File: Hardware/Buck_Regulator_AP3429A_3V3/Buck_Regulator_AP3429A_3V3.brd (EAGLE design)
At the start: 25.4 x 25.4 mm, 51 parts, among them J1 Screw Terminal, J2 POWER_JACKPOWER_JACK_SLOT_COM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, J3 Breakout Headers, U1 AP3429/A

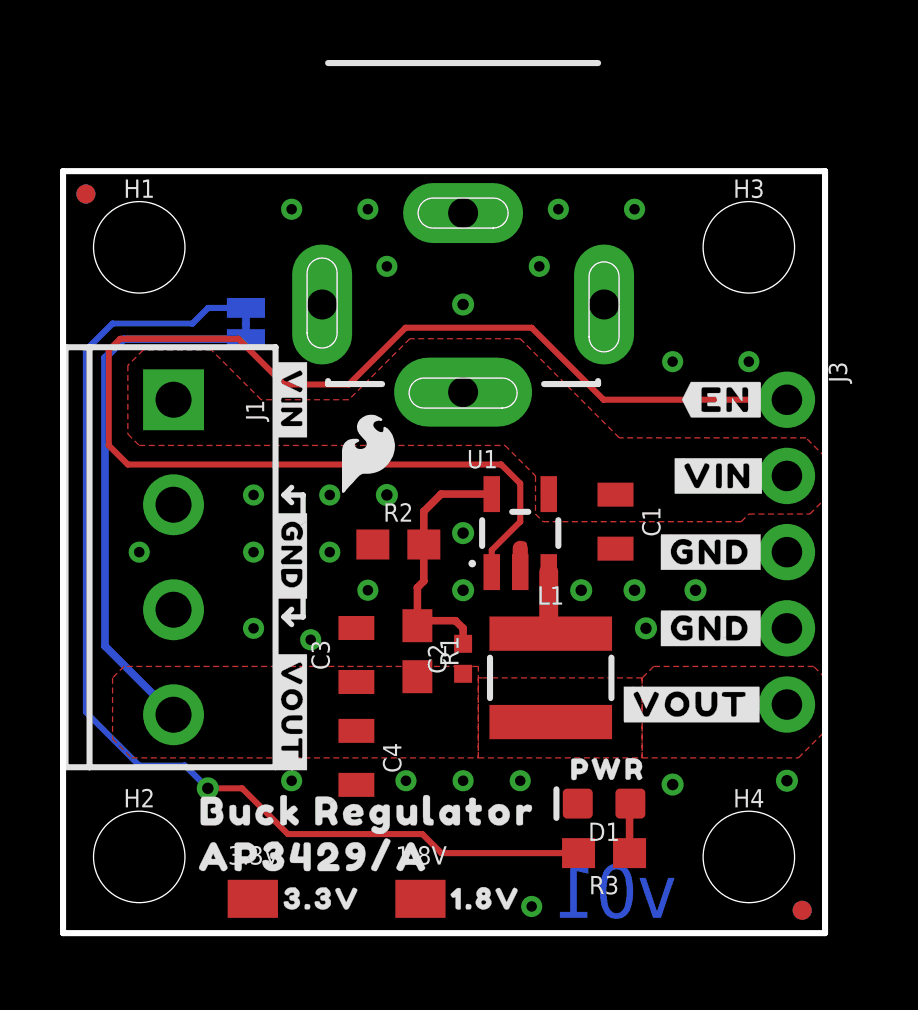
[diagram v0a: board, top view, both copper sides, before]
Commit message: Updated 3.3V files to be the same as 1.8V
Changed the 3 resistors (R1, R2, R3) and placed them in the same location as the 1.8V board files.
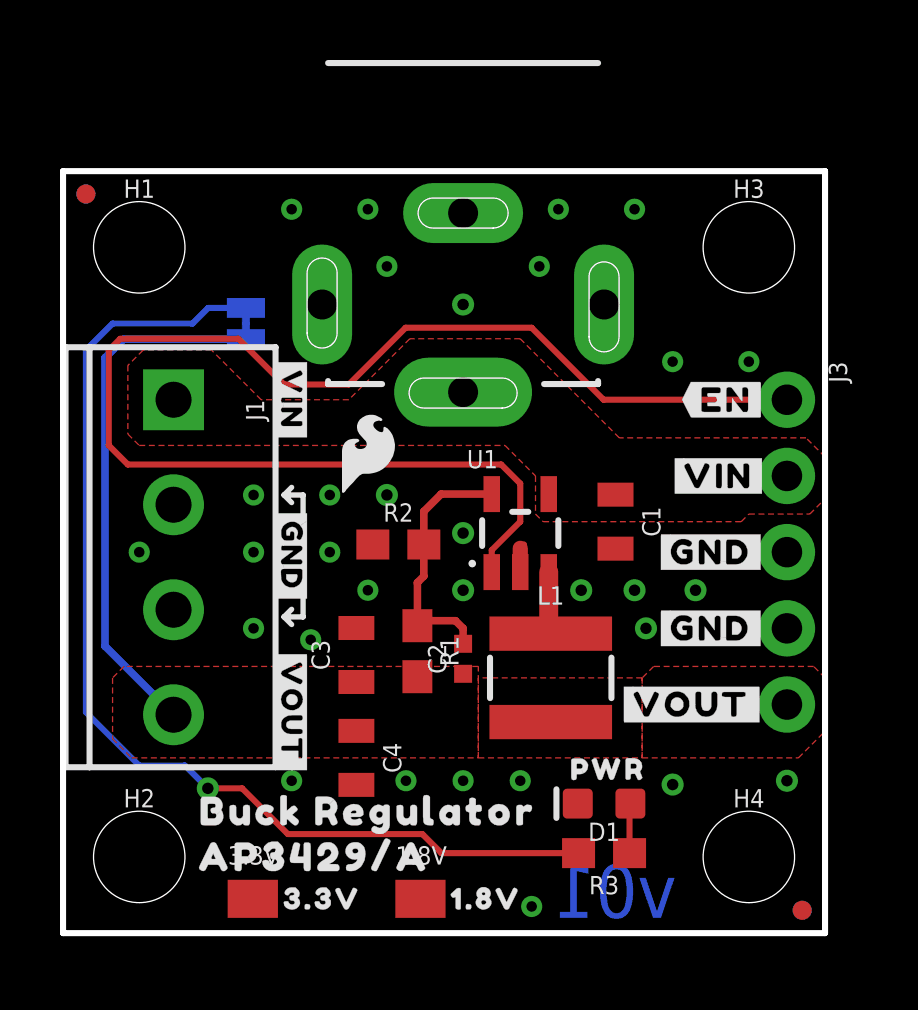
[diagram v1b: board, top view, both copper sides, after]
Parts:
- 1.8V: value PROD_ID_PASTE_NO-SILK -> PROD_ID_NO-PASTE_NO_SILK; device SparkFun-Aesthetics:PRODUCT_IDENT_PASTE_NO-SILK -> SparkFun-Aesthetics:PRODUCT_IDENT_NO_NO-SILK
- 3.3V: value PROD_ID_NO-PASTE_NO_SILK -> PROD_ID_PASTE_NO-SILK; device SparkFun-Aesthetics:PRODUCT_IDENT_NO_NO-SILK -> SparkFun-Aesthetics:PRODUCT_IDENT_PASTE_NO-SILK
- R1: value 300k -> 453k
- R2: value 150k -> 100k
- R3: value 100 -> 1k
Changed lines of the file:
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@@
 <drawing>
 <settings>
-<setting alwaysvectorfont="yes"/>
+<setting alwaysvectorfont="no"/>
 <setting verticaltext="up"/>
 </settings>
@@
 <layer number="44" name="Drills" color="7" fill="1" visible="no" active="yes"/>
 <layer number="45" name="Holes" color="7" fill="1" visible="yes" active="yes"/>
-<layer number="46" name="Milling" color="3" fill="1" visible="no" active="yes"/>
+<layer number="46" name="Milling" color="3" fill="1" visible="yes" active="yes"/>
 <layer number="47" name="Measures" color="7" fill="1" visible="no" active="yes"/>
 <layer number="48" name="Document" color="7" fill="1" visible="no" active="yes"/>
@@
 <attribute name="NAME" x="4.953" y="20.32" size="0.6096" layer="26" font="vector" ratio="20" rot="MR270" align="bottom-center"/>
 </element>
-<element name="R1" library="SparkFun-Resistors" package="0603" value="300k" x="11.811" y="9.398" smashed="yes" rot="R270">
-<attribute name="NAME" x="12.573" y="9.398" size="0.6096" layer="25" font="vector" ratio="20" rot="R270" align="bottom-center"/>
-<attribute name="PROD_ID" value="RES-10809" x="-22.479" y="-42.672" size="1.778" layer="27" rot="R270" display="off"/>
-</element>
-<element name="R2" library="SparkFun-Resistors" package="0603" value="150k" x="11.176" y="12.954" smashed="yes">
-<attribute name="NAME" x="11.176" y="13.716" size="0.6096" layer="25" font="vector" ratio="20" align="bottom-center"/>
-<attribute name="PROD_ID" value="RES-09117" x="26.416" y="-26.416" size="1.778" layer="27" display="off"/>
-</element>
-<element name="R3" library="SparkFun-Resistors" package="0603" value="100" x="18.034" y="2.667" smashed="yes" rot="R180">
-<attribute name="NAME" x="18.034" y="1.905" size="0.6096" layer="25" font="vector" ratio="20" rot="R180" align="bottom-center"/>
-<attribute name="PROD_ID" value="RES-07863" x="-1.016" y="42.037" size="1.778" layer="27" rot="R180" display="off"/>
-</element>
 <element name="U1" library="SparkFun-IC-Power" package="SOT23-5" value="AP3429/A" x="15.24" y="13.335" smashed="yes">
 <attribute name="NAME" x="13.462" y="15.494" size="0.6096" layer="25" ratio="20"/>
@@
 <attribute name="VALUE" x="1.397" y="17.78" size="0.6096" layer="27" font="vector" ratio="20" rot="R270"/>
 </element>
-<element name="3.3V" library="SparkFun-Aesthetics" package="PRODUCT_IDENT_NO_NO-SILK" value="PROD_ID_NO-PASTE_NO_SILK" x="6.35" y="1.143" smashed="yes">
+<element name="1.8V" library="SparkFun-Aesthetics" package="PRODUCT_IDENT_NO_NO-SILK" value="PROD_ID_NO-PASTE_NO_SILK" x="11.938" y="1.143" smashed="yes">
+<attribute name="NAME" x="11.938" y="2.286" size="0.6096" layer="25" font="vector" ratio="20" align="bottom-center"/>
+<attribute name="VALUE" x="11.938" y="0" size="0.6096" layer="27" font="vector" ratio="20" align="top-center"/>
+</element>
+<element name="3.3V" library="SparkFun-Aesthetics" package="PRODUCT_IDENT_PASTE_NO-SILK" value="PROD_ID_PASTE_NO-SILK" x="6.35" y="1.143" smashed="yes">
 <attribute name="NAME" x="6.35" y="2.286" size="0.6096" layer="25" font="vector" ratio="20" align="bottom-center"/>
 <attribute name="VALUE" x="6.35" y="0" size="0.6096" layer="27" font="vector" ratio="20" align="top-center"/>
-</element>
-<element name="1.8V" library="SparkFun-Aesthetics" package="PRODUCT_IDENT_PASTE_NO-SILK" value="PROD_ID_PASTE_NO-SILK" x="11.938" y="1.143" smashed="yes">
-<attribute name="NAME" x="11.938" y="2.286" size="0.6096" layer="25" font="vector" ratio="20" align="bottom-center"/>
-<attribute name="VALUE" x="11.938" y="0" size="0.6096" layer="27" font="vector" ratio="20" align="top-center"/>
 </element>
 <element name="U$23" library="output" package="3#3V3441" value="" x="8.636" y="1.143" smashed="yes"/>
@@
 <element name="J2" library="SparkFun-Connectors" package="POWER_JACK_PTH_SLOT_BOTH" value="POWER_JACKPOWER_JACK_SLOT_COMBO" x="13.335" y="24.003" smashed="yes" rot="R90"/>
 <element name="U$16" library="output" package="BUCK_REGULATOR_AP3429#A3453" value="" x="1.524" y="12.827" smashed="yes" rot="MR90"/>
+<element name="R1" library="SparkFun-Resistors" package="0603" value="453k" x="11.811" y="9.398" smashed="yes" rot="R270">
+<attribute name="NAME" x="12.573" y="9.398" size="0.6096" layer="25" font="vector" ratio="20" rot="R270" align="bottom-center"/>
+<attribute name="PROD_ID" value="RES-14466" x="11.811" y="9.398" size="1.778" layer="27" rot="R270" display="off"/>
+<attribute name="VALUE" x="11.049" y="9.398" size="0.6096" layer="27" font="vector" ratio="20" rot="R270" align="top-center"/>
+</element>
+<element name="R2" library="SparkFun-Resistors" package="0603" value="100k" x="11.176" y="12.954" smashed="yes">
+<attribute name="NAME" x="11.176" y="13.716" size="0.6096" layer="25" font="vector" ratio="20" align="bottom-center"/>
+<attribute name="PROD_ID" value="RES-07828" x="11.176" y="12.954" size="1.778" layer="27" display="off"/>
+<attribute name="VALUE" x="11.176" y="12.192" size="0.6096" layer="27" font="vector" ratio="20" align="top-center"/>
+</element>
+<element name="R3" library="SparkFun-Resistors" package="0603" value="1k" x="18.034" y="2.667" smashed="yes" rot="R180">
+<attribute name="NAME" x="18.034" y="1.905" size="0.6096" layer="25" font="vector" ratio="20" rot="R180" align="bottom-center"/>
+<attribute name="PROD_ID" value="RES-07856" x="18.034" y="2.667" size="1.778" layer="27" rot="R180" display="off"/>
+<attribute name="VALUE" x="18.034" y="3.429" size="0.6096" layer="27" font="vector" ratio="20" rot="R180" align="top-center"/>
+</element>
 </elements>
 <signals>
@@
 <signal name="GND">
 <contactref element="U1" pad="2"/>
-<contactref element="R2" pad="1"/>
 <contactref element="D1" pad="C"/>
 <contactref element="J3" pad="3"/>
@@
 <via x="16.51" y="24.13" extent="1-16" drill="0.35"/>
 <via x="10.16" y="24.13" extent="1-16" drill="0.35"/>
+<contactref element="R2" pad="1"/>
 </signal>
 <signal name="N$1">
@@
 <signal name="N$2">
 <contactref element="U1" pad="5"/>
-<contactref element="R1" pad="1"/>
-<contactref element="R2" pad="2"/>
 <contactref element="C2" pad="2"/>
 <wire x1="14.29" y1="14.6351" x2="12.6031" y2="14.6351" width="0.254" layer="1"/>
-<wire x1="12.026" y1="14.058" x2="12.026" y2="12.954" width="0.254" layer="1"/>
-<wire x1="12.6031" y1="14.6351" x2="12.026" y2="14.058" width="0.254" layer="1"/>
-<wire x1="12.026" y1="11.733" x2="11.811" y2="11.518" width="0.254" layer="1"/>
-<wire x1="11.811" y1="10.248" x2="11.811" y2="11.518" width="0.254" layer="1"/>
-<wire x1="12.026" y1="11.733" x2="12.026" y2="12.954" width="0.254" layer="1"/>
+<wire x1="12.026" y1="14.058" x2="12.6031" y2="14.6351" width="0.254" layer="1"/>
 <wire x1="12.025984375" y1="10.414" x2="13.081" y2="10.414" width="0.254" layer="1"/>
 <wire x1="13.081" y1="10.414" x2="13.335" y2="10.16" width="0.254" layer="1"/>
 <wire x1="13.335" y1="10.16" x2="13.335" y2="9.644" width="0.254" layer="1"/>
-<wire x1="11.85998125" y1="10.247996875" x2="12.025984375" y2="10.414" width="0.2032" layer="1"/>
-<wire x1="11.811" y1="10.248" x2="11.859978125" y2="10.248" width="0.1778" layer="1"/>
-<wire x1="11.859978125" y1="10.248" x2="11.85998125" y2="10.247996875" width="0.1778" layer="1"/>
+<wire x1="12.025984375" y1="10.414" x2="11.85998125" y2="10.247996875" width="0.2032" layer="1"/>
+<contactref element="R1" pad="1"/>
+<contactref element="R2" pad="2"/>
+<wire x1="12.026" y1="12.954" x2="12.026" y2="14.058" width="0.254" layer="1"/>
+<wire x1="11.811" y1="10.248" x2="11.811" y2="11.684" width="0.254" layer="1"/>
+<wire x1="12.026" y1="11.899" x2="12.026" y2="12.954" width="0.254" layer="1"/>
+<wire x1="11.811" y1="11.684" x2="12.026" y2="11.899" width="0.254" layer="1"/>
+<wire x1="11.811" y1="10.248" x2="11.859978125" y2="10.248" width="0.2032" layer="1"/>
+<wire x1="11.859978125" y1="10.248" x2="11.85998125" y2="10.247996875" width="0.2032" layer="1"/>
 </signal>
 <signal name="EN">
@@
 <signal name="N$3">
 <contactref element="PWR" pad="1"/>
-<contactref element="R3" pad="2"/>
 <wire x1="6.096" y1="20.8407" x2="4.8387" y2="20.8407" width="0.2032" layer="16"/>
 <wire x1="1.651" y1="20.32" x2="0.762" y2="19.431" width="0.2032" layer="16"/>
 <wire x1="4.8387" y1="20.8407" x2="4.318" y2="20.32" width="0.2032" layer="16"/>
 <wire x1="4.318" y1="20.32" x2="1.651" y2="20.32" width="0.2032" layer="16"/>
-<wire x1="12.612" y1="2.667" x2="17.184" y2="2.667" width="0.2032" layer="1"/>
-<wire x1="12.612" y1="2.667" x2="11.977" y2="3.302" width="0.2032" layer="1"/>
+<wire x1="11.977" y1="3.302" x2="12.612" y2="2.667" width="0.2032" layer="1"/>
 <wire x1="11.977" y1="3.302" x2="7.493" y2="3.302" width="0.2032" layer="1"/>
 <via x="4.826" y="4.826" extent="1-16" drill="0.381"/>
@@
 <wire x1="4.064" y1="5.588" x2="4.826" y2="4.826" width="0.2032" layer="16"/>
 <wire x1="4.064" y1="5.588" x2="2.54" y2="5.588" width="0.2032" layer="16"/>
+<contactref element="R3" pad="2"/>
+<wire x1="12.612" y1="2.667" x2="17.184" y2="2.667" width="0.2032" layer="1"/>
 </signal>
 <signal name="N$4">
 <contactref element="D1" pad="A"/>
+<wire x1="18.911" y1="4.318" x2="18.884" y2="4.291" width="0.254" layer="1"/>
 <contactref element="R3" pad="1"/>
-<wire x1="18.911" y1="4.318" x2="18.884" y2="4.291" width="0.254" layer="1"/>
-<wire x1="18.884" y1="4.291" x2="18.884" y2="2.667" width="0.254" layer="1"/>
+<wire x1="18.884" y1="2.667" x2="18.884" y2="4.291" width="0.2032" layer="1"/>
 </signal>
 <signal name="VOUT">
@@
 <wire x1="2.0193" y1="19.7993" x2="1.397" y2="19.177" width="0.254" layer="16"/>
 <contactref element="L1" pad="P$2"/>
-<contactref element="R1" pad="2"/>
 <contactref element="C2" pad="1"/>
 <wire x1="1.397" y1="9.566" x2="3.683" y2="7.28" width="0.254" layer="16"/>
@@
 <vertex x="19.304" y="5.842"/>
 <vertex x="19.304" y="8.509"/>
-<vertex x="13.97" y="8.509"/>
 <vertex x="13.843" y="8.509"/>
 </polygon>
@@
 <vertex x="19.304" y="8.509"/>
 </polygon>
+<contactref element="R1" pad="2"/>
 </signal>
 </signals>

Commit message: Nudge traces for better GND pour connection on BRD
Moved some traces for a better GND pour on the top layer.
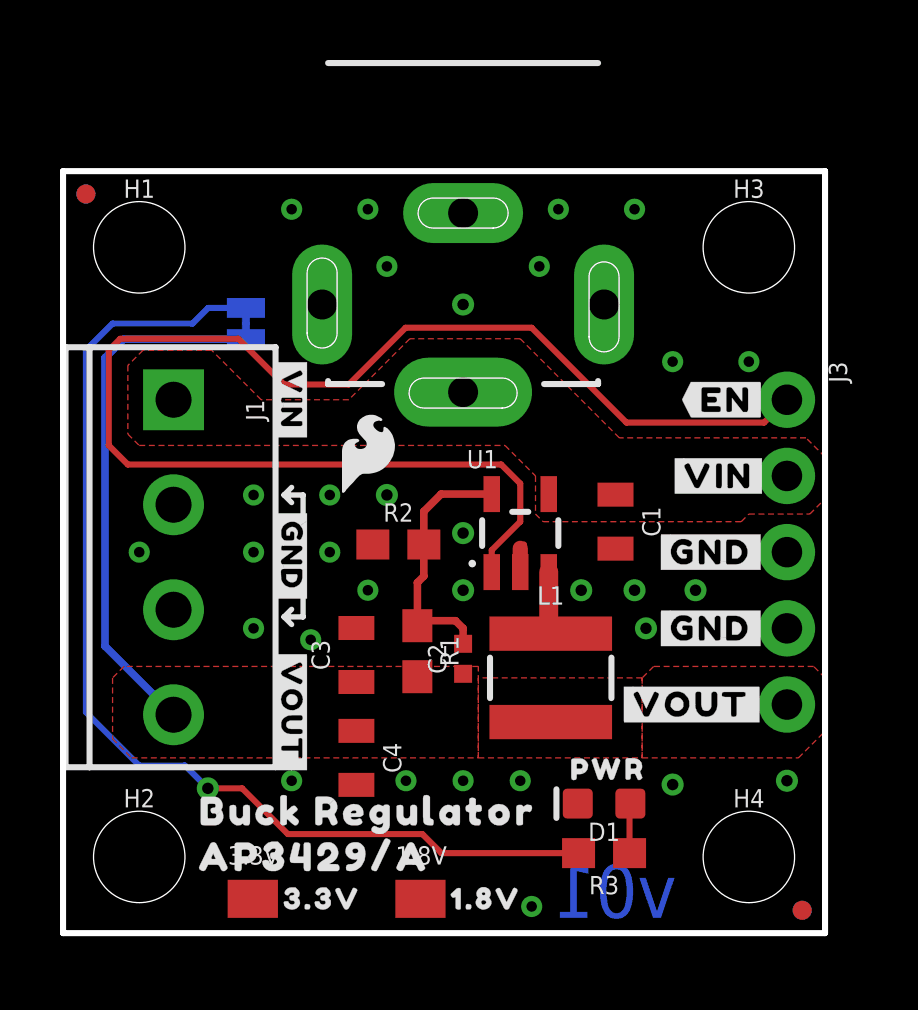
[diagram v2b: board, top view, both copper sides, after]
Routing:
- net EN: track 45.9 -> 46.6 mm
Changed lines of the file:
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@@
 <layer number="44" name="Drills" color="7" fill="1" visible="no" active="yes"/>
 <layer number="45" name="Holes" color="7" fill="1" visible="yes" active="yes"/>
-<layer number="46" name="Milling" color="3" fill="1" visible="yes" active="yes"/>
+<layer number="46" name="Milling" color="3" fill="1" visible="no" active="yes"/>
 <layer number="47" name="Measures" color="7" fill="1" visible="no" active="yes"/>
 <layer number="48" name="Document" color="7" fill="1" visible="no" active="yes"/>
@@
 <wire x1="1.524" y1="16.256" x2="1.524" y2="19.431" width="0.2032" layer="1"/>
 <wire x1="1.524" y1="19.431" x2="1.905" y2="19.812" width="0.2032" layer="1"/>
-<wire x1="15.61835" y1="20.1803" x2="18.01865" y2="17.78" width="0.2032" layer="1"/>
+<wire x1="15.61835" y1="20.1803" x2="18.78065" y2="17.018" width="0.2032" layer="1"/>
 <wire x1="1.905" y1="19.812" x2="5.842" y2="19.812" width="0.2032" layer="1"/>
 <wire x1="5.842" y1="19.812" x2="7.366" y2="18.288" width="0.2032" layer="1"/>
@@
 <wire x1="9.525" y1="18.288" x2="11.4173" y2="20.1803" width="0.2032" layer="1"/>
 <wire x1="11.4173" y1="20.1803" x2="15.61835" y2="20.1803" width="0.2032" layer="1"/>
-<wire x1="24.13" y1="17.78" x2="18.01865" y2="17.78" width="0.2032" layer="1"/>
+<wire x1="24.13" y1="17.78" x2="23.368" y2="17.018" width="0.2032" layer="1"/>
+<wire x1="23.368" y1="17.018" x2="18.78065" y2="17.018" width="0.2032" layer="1"/>
 </signal>
 <signal name="N$3">
